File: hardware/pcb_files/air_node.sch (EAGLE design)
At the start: 31 parts, among them X1 RASPI_BOARD_B+#_E4

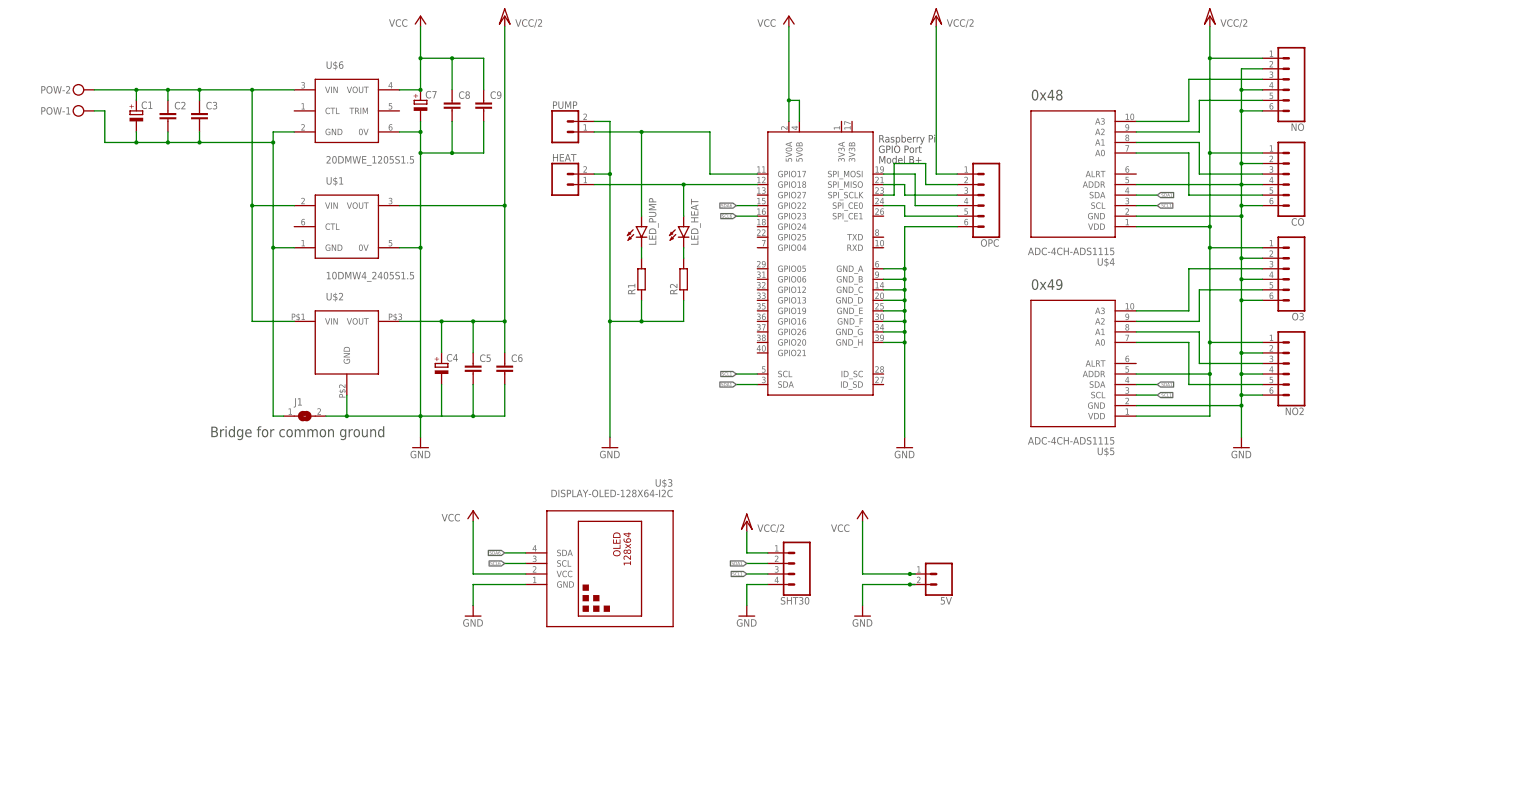
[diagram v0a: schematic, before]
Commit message: pcb v0.2
added one-wire, uart, usb disconnector port and one more ads1115
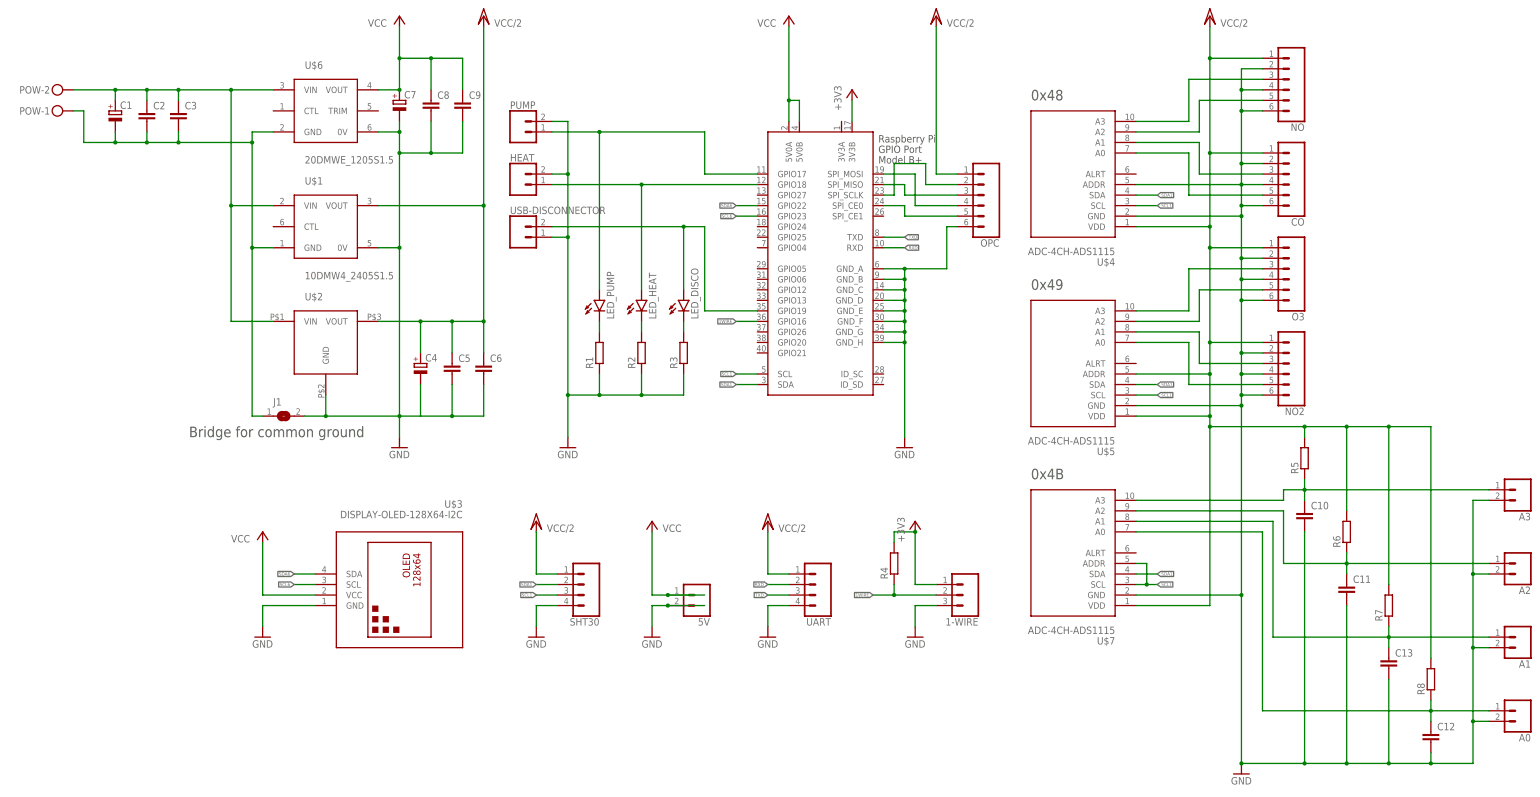
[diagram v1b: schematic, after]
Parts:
- added 1-WIRE: (no value), SparkFun-Connectors:CONN_031X03_NO_SILK
- added A0, A1, A2, A3, USB-DISCONNECTOR: (no value), SparkFun-Connectors:CONN_021X02_NO_SILK
- added C10, C11, C12, C13: (no value), rcl:C-EUC0805
- added LED_DISCO: (no value), led:LEDCHIP-LED0805
- added R3, R4, R5, R6, R7, R8: (no value), rcl:R-EU_R0805
- added U$7: ADC-4CH-ADS1115, diy-modules:ADC-4CH-ADS1115
- added UART: (no value), SparkFun-Connectors:CONN_041X04_NO_SILK
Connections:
- new net +3V3: 1-WIRE.1, R4.2, X1.3V3B
- new net 1WIRE: 1-WIRE.2, R4.1, X1.GPIO16
- new net N$17: A1.1, C13.1, R7.1, U$7.A1
- new net N$18: LED_DISCO.A, USB-DISCONNECTOR.2, X1.GPIO19
- new net N$19: A0.1, C12.1, R8.1, U$7.A0
- new net N$20: A3.1, C10.1, R5.1, U$7.A3
- new net N$21: A2.1, C11.1, R6.1, U$7.A2
- new net N$22: LED_DISCO.C, R3.2
- new net RXD: UART.2, X1.RXD
- new net TXD: UART.3, X1.TXD
- net GND: now also 1-WIRE.3, A0.2, A1.2, A2.2, A3.2, C10.2, C11.2, C12.2, C13.2, R3.1, U$7.GND, UART.4, USB-DISCONNECTOR.1
- net SCL1: now also U$7.ADDR, U$7.SCL
- net SDA1: now also U$7.SDA
- net VCC/2: now also R5.2, R6.2, R7.2, R8.2, U$7.VDD, UART.1
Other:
- note added: "0x4B"
- moved on the sheet: 5V, C1, C2, C3, C4, C5, C6, C7, C8, C9, HEAT, J1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
